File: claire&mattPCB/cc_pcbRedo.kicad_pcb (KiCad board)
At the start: 2 copper layers, 145.2 x 105.1 mm, 89 parts, among them J1 Conn_02x05_Odd_Even, J2 Micro_SD_Card_Det_Hirose_DM3AT, J3 4x4 Keypad, J4 DC-DC_JUMPER, J5 PS_WIRES, J6 PS_BJ, J7 DC-DC Converter, SW1 SW_Push, U1 ESP8266, U2 7in_display_controller, U3 RFID_Scanner, U4 TFT_2.8IN_DISPLAY, U5 74HC14, U6 STM32F091RCTx, U7 MEZD71201AF, U8 TPS56325x, U9 4N28

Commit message: minor changes
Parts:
- added R29: 0, Resistor_SMD:R_0805_2012Metric_Pad1.20x1.40mm_HandSolder, F.Cu at (184.4, 77.7)
- C11, C12: moved to F.Cu
- moved H4 3.34 mm to (82.5, 47.4)
- moved H1 2.14 mm to (82.5, 127.4)
- moved C12 1.59 mm to (176.0, 113.0)
- moved R5 1.42 mm to (122.4, 63.0), turned to 0 degrees
- moved H2 1.39 mm to (207.5, 127.4)
- moved H3 1.31 mm to (207.5, 47.4)
- moved R27 1.18 mm to (140.3, 76.2), turned to 90 degrees
- moved C8 0.87 mm to (122.5, 60.3), turned to 180 degrees
- moved C11 0.83 mm to (176.0, 110.8)
- moved L2 0.75 mm to (172.5, 108.0)
- moved C13 0.15 mm to (174.2, 103.3)
- moved C14 0.15 mm to (174.2, 101.1)
- turned R26 to 90 degrees
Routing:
- net +5V: track 105.7 -> 332.6 mm
- net GND: track 69.8 -> 167.5 mm, vias 10 -> 12
- net +3V3: track 73.9 -> 98.1 mm, vias 5 -> 9
- net 9_GND: track 24.9 -> 39.8 mm, vias 0 -> 1
- net DC_DES: track 11.7 -> 14.5 mm
- net PB14: track 76.8 -> 74.3 mm
- net PB11: track 56.4 -> 57.5 mm
- net Net-(R26-Pad2): track 7.17 -> 6.38 mm
- net /NRST: track 44.6 -> 45.3 mm
- added copper zone on F.Cu, net +3V3
- added copper zone on F.Cu, net GND
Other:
- board size 145.2 x 105.1 mm -> 146.1 x 101.6 mm

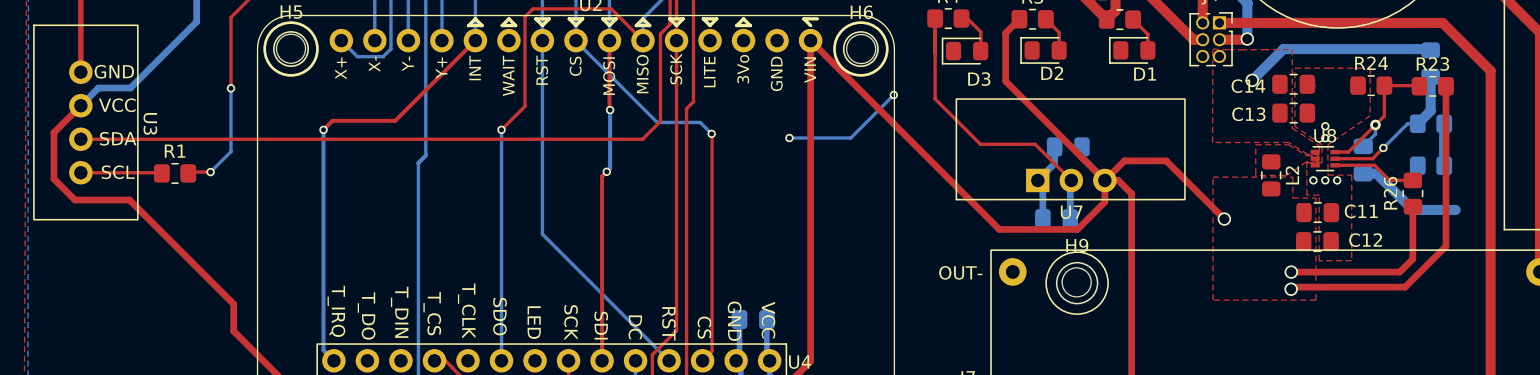
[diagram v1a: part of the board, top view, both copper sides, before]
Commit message: updated schematic with text descriptions for each block. Also, added 0 ohm resistor and 10 ohm current limiting resistor to pcb. Minor changes were made to the designed buck converter circuit.
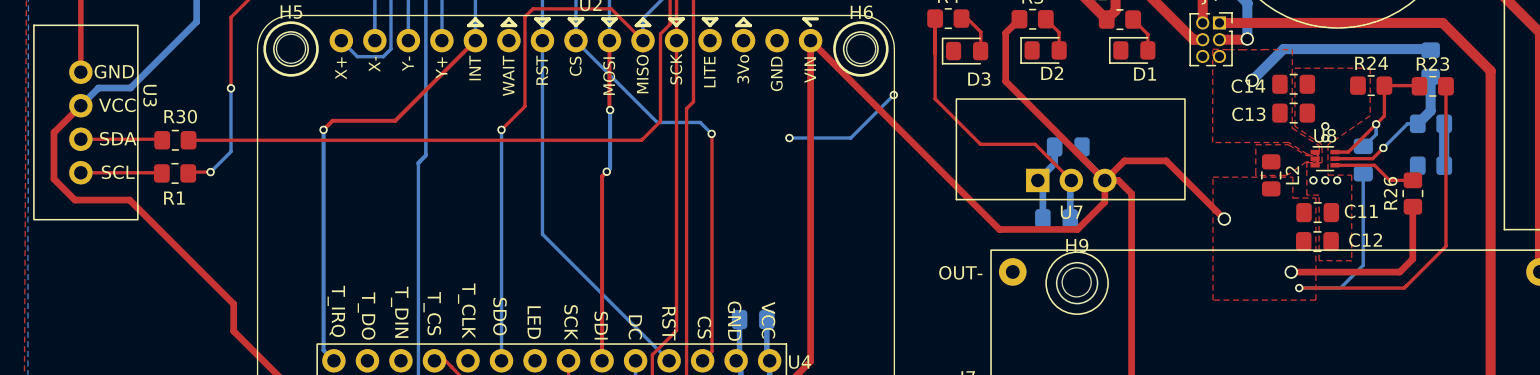
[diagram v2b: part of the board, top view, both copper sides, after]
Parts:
- added R30: 10, Resistor_SMD:R_0805_2012Metric_Pad1.20x1.40mm_HandSolder, F.Cu at (89.5, 105.4)
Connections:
- U3 pad 3: PD2 -> Net-(U3-Pad3)
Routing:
- net PD2: track 67.9 -> 59.8 mm
- net Net-(U3-Pad3): track 0.00 -> 6.19 mm
- net +5V: track 332.6 -> 336.5 mm

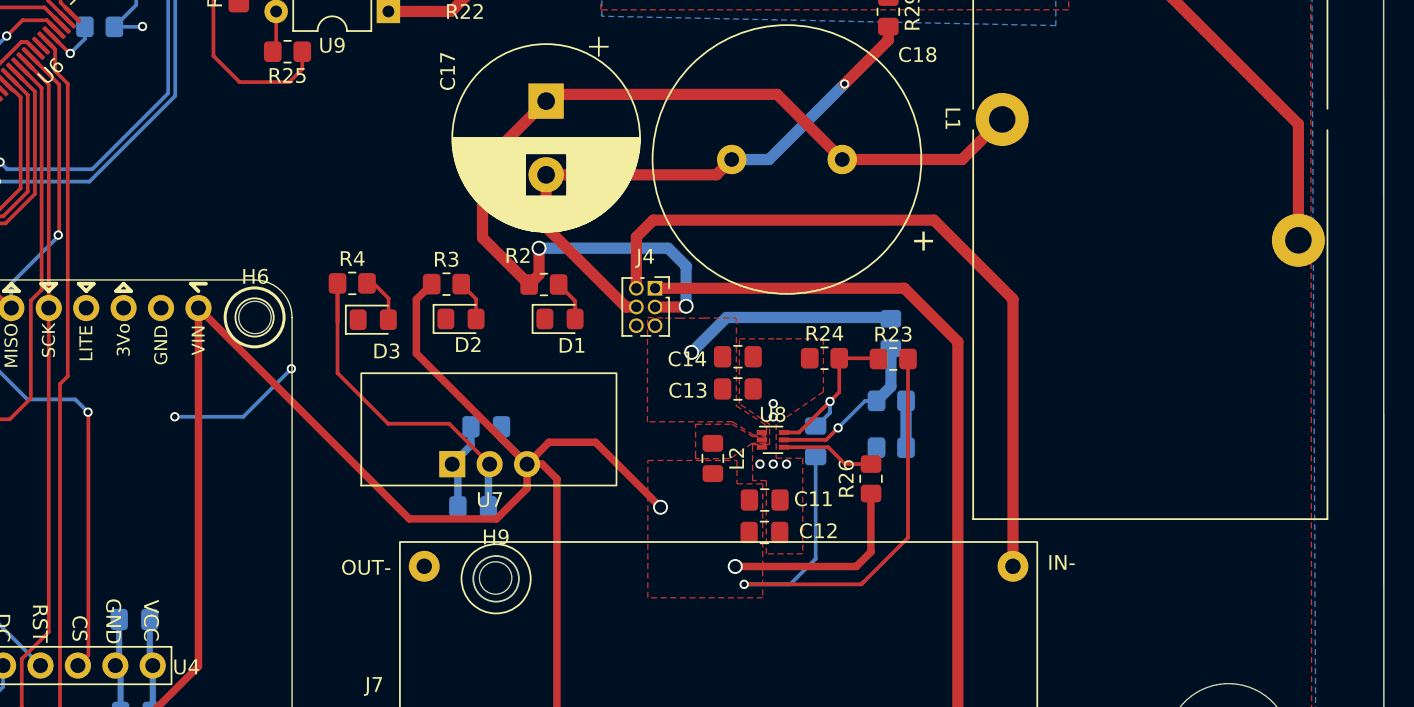
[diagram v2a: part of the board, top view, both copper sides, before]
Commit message: added fantabulous silkscreen names to the board (schmack dab in the middle)
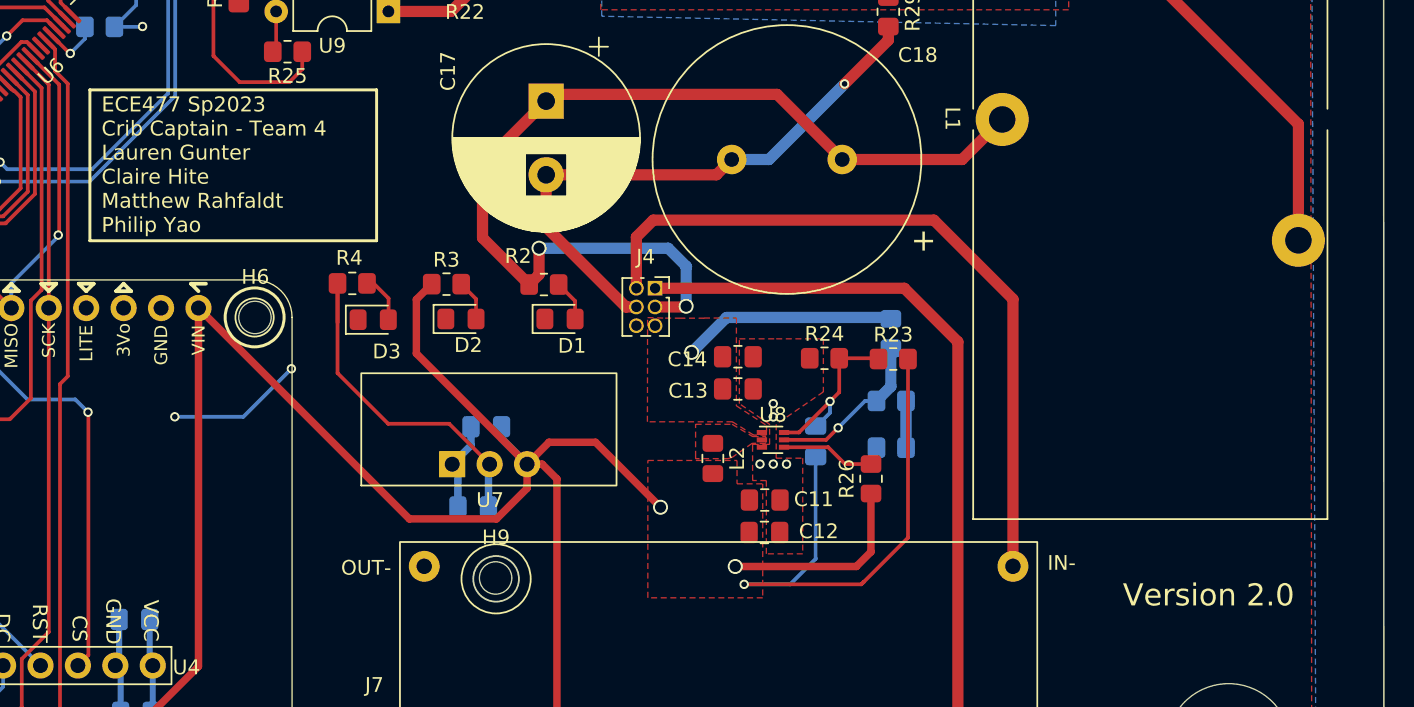
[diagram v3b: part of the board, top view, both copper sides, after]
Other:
- board text added: "ECE477 Sp2023 Crib Captain - Team 4 Lauren Gunter Claire Hite Matthew Rahfaldt Philip Yao"
- board text added: "Version 2.0"
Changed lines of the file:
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@@
     (property "Sheetname" "")
     (attr smd)
-    (fp_text reference "R4" (at 0 -1.65) (layer "F.SilkS")
+    (fp_text reference "R4" (at -0.2032 -1.7272) (layer "F.SilkS")
       (effects (font (size 1 1) (thickness 0.15)))
     )
@@
   )
   (gr_circle (center 130.826559 75.098221) (end 130.826559 75.707821) (layer "F.SilkS") (width 0.15) (fill none))
+  (gr_rect (start 130.2258 83.0072) (end 149.6822 93.2434) (layer "F.SilkS") (width 0.2) (fill none))
   (gr_line (start 209.67 137.94) (end 80.473451 137.94) (layer "Edge.Cuts") (width 0.1))
   (gr_arc (start 209.617374 36.352626) (mid 215.55 38.81) (end 218.007374 44.742626) (layer "Edge.Cuts") (width 0.1))
@@
     (effects (font (size 1.5 1.5) (thickness 0.3)))
   )
+  (gr_text "ECE477 Sp2023\nCrib Captain - Team 4 \nLauren Gunter\nClaire Hite\nMatthew Rahfaldt\nPhilip Yao" (at 131.0132 88.0872) (layer "F.SilkS")
+    (effects (font (size 1.016 1.016) (thickness 0.1905)) (justify left))
+  )
+  (gr_text "Version 2.0" (at 206.1464 117.2972) (layer "F.SilkS")
+    (effects (font (size 1.5 1.5) (thickness 0.3)))
+  )

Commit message: no DRC warnings
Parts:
- moved C12 0.29 mm to (176.0, 112.8)
- moved C11 0.10 mm to (176.0, 110.7)
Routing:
- net +3V3: track 98.1 -> 118.8 mm
- net GND: track 167.3 -> 184.4 mm, vias 12 -> 13
- net PB5: track 45.8 -> 62.5 mm
- net PB4: track 57.0 -> 70.0 mm
- net PB3: track 54.9 -> 64.5 mm
- net VAC_GND: track 37.8 -> 47.3 mm
- net PB14: track 74.3 -> 71.7 mm
- net PB7: track 71.4 -> 73.1 mm

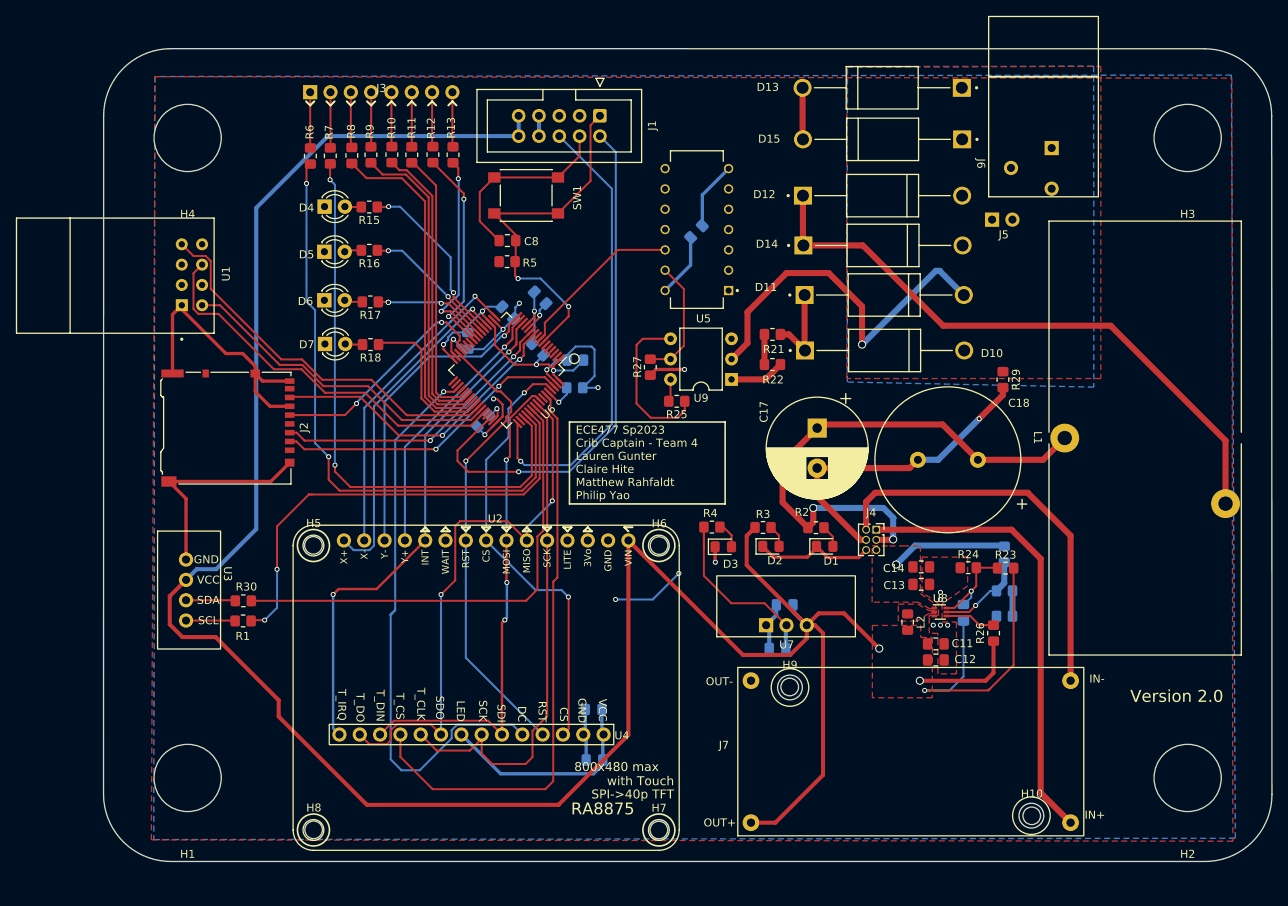
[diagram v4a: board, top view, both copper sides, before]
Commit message: diodes and vias w labels added
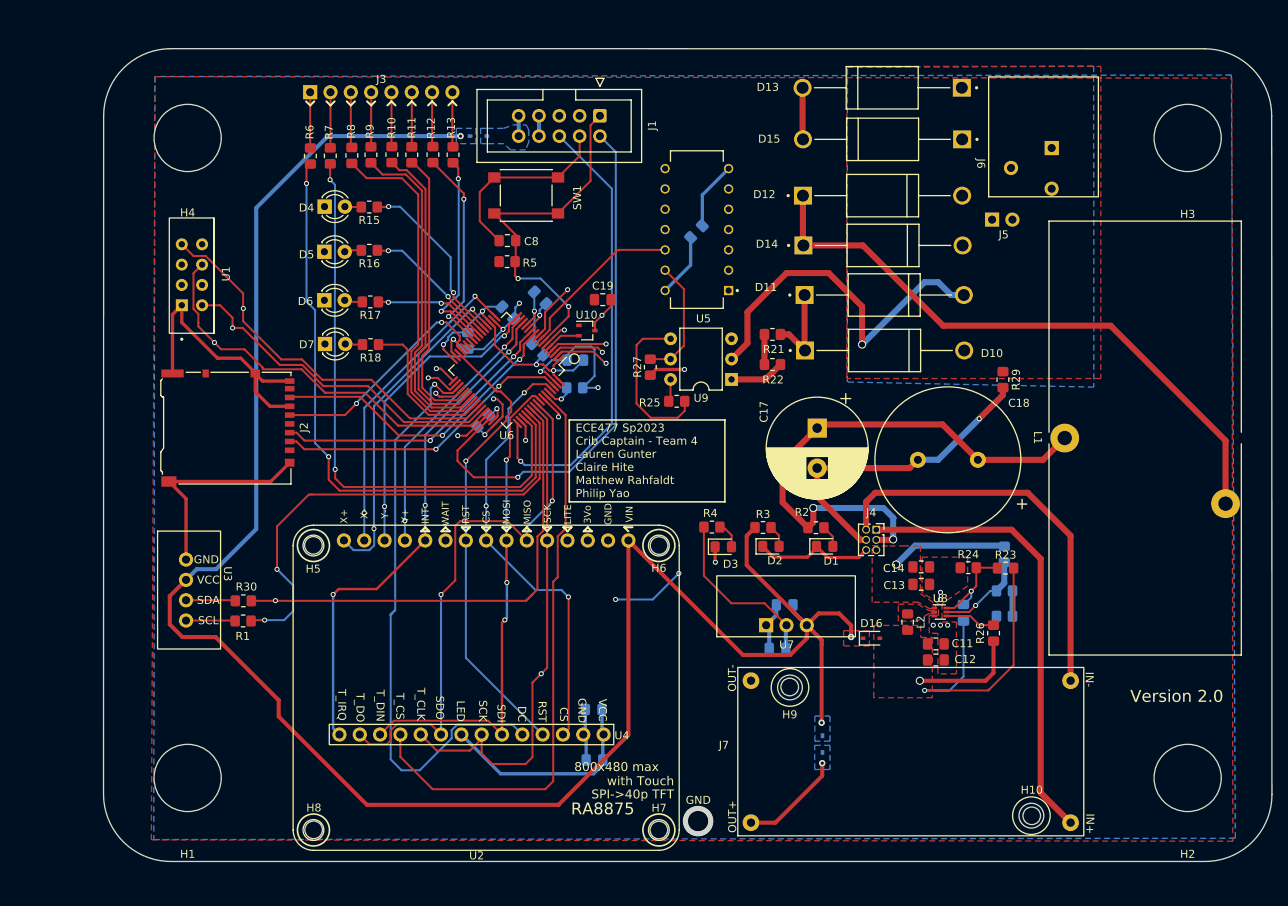
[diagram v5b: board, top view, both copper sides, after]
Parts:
- added C19: .1uF, Capacitor_SMD:C_0805_2012Metric_Pad1.18x1.45mm_HandSolder, F.Cu at (134.4, 67.7)
- added D16: BAT60JFILM, Diode_SMD:D_SOD-323, F.Cu at (168.0, 110.0)
- added D8: BAT60JFILM, Diode_SMD:D_SOD-323, B.Cu at (118.8, 47.3)
- added D9: BAT60JFILM, Diode_SMD:D_SOD-323, B.Cu at (161.8, 123.3)
- added U10: MAX7375AXR805, Package_TO_SOT_SMD:SOT-323_SC-70, F.Cu at (132.4, 71.6)
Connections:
- C11 pad 1: +5V -> Net-(C11-Pad1)
- C12 pad 1: +5V -> Net-(C11-Pad1)
- C16 pad 1: +5V -> Net-(C11-Pad1)
- J1 pad 10: +5V -> /U5V
- J1 pad 9: +5V -> /U5V
- J7 pad 3: +5V -> Net-(J7-Pad3)
- L2 pad 2: +5V -> Net-(C11-Pad1)
- R23 pad 2: +5V -> Net-(C11-Pad1)
- R26 pad 1: +5V -> Net-(C11-Pad1)
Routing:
- net +5V: track 336.5 -> 253.9 mm
- net Net-(C11-Pad1): track 0.00 -> 50.8 mm, vias 0 -> 2
- net Net-(J7-Pad3): track 0.00 -> 12.9 mm, vias 0 -> 1
- net /PC1: track 0.00 -> 7.43 mm, vias 0 -> 1
- net /PC15: track 0.00 -> 7.19 mm, vias 0 -> 1
- net /PC13: track 0.00 -> 6.98 mm, vias 0 -> 1
- net /PC14: track 0.00 -> 6.57 mm, vias 0 -> 1
- net GND: track 184.4 -> 190.7 mm, vias 13 -> 15
- net PC10: track 79.0 -> 73.2 mm
- net /PA12: track 0.00 -> 4.76 mm, vias 0 -> 1
- net /PF0: track 0.00 -> 4.42 mm
- net /PB13: track 0.00 -> 4.37 mm, vias 0 -> 1
- net /PB15: track 0.00 -> 3.79 mm, vias 0 -> 1
- net /PB6: track 0.00 -> 3.17 mm, vias 0 -> 1
- net /PF1: track 0.00 -> 3.11 mm, vias 0 -> 1
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- added copper zone on B.Cu, net +5V
- added copper zone on B.Cu, net /U5V
- added copper zone on F.Cu, net Net-(C11-Pad1)
- added copper zone on B.Cu, net Net-(J7-Pad3)
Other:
- board text added: "GND"
- board text added: "PA0"
- board text added: "PA1"
- board text added: "PA10"
- board text added: "PA11"
- board text added: "PA12"
- board text added: "PA13"
- board text added: "PA14"
- board text added: "PA15"
- board text added: "PA2"
- board text added: "PA3"
- board text added: "PA4"
- board text added: "PA9"
- board text added: "PB10"
- board text added: "PB11"
- board text added: "PB12"
- board text added: "PB13"
- board text added: "PB14"
- board text added: "PB15"
- board text added: "PB3"
- board text added: "PB4"
- board text added: "PB5"
- board text added: "PB6"
- board text added: "PB8"
- board text added: "PB9"
- board text added: "PC1"
- board text added: "PC10"
- board text added: "PC11"
- board text added: "PC12"
- board text added: "PC13"
- board text added: "PC14"
- board text added: "PC15"
- board text added: "PC2"
- board text added: "PC3"
- board text added: "PD2"
- board text added: "PF1"
- board text added: "RST"
- board text added: "RX"
- board text added: "TX"

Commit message: pcb finalization
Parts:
- J4: footprint Connector_PinSocket_1.27mm:PinSocket_2x03_P1.27mm_Vertical -> Connector_PinSocket_2.54mm:PinSocket_2x03_P2.54mm_Vertical
- moved J4 1.17 mm to (168.4, 95.3)
- moved H10 0.36 mm to (188.2, 132.6)
- moved H9 0.35 mm to (157.6, 115.8)
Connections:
- U5 pad 12: PC0 -> PC13
- U6 pad 2: /PC13 -> PC13
- U6 pad 8: PC0 -> /PC0
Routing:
- net PC13: track 0.00 -> 24.2 mm, vias 0 -> 1
- net PC0: track 21.1 -> 0.00 mm
- net /PC13: track 6.98 -> 0.00 mm, vias 1 -> 0
- net +3V3: track 116.0 -> 121.4 mm
- net /PC1: track 7.43 -> 5.72 mm
- net GND: track 190.7 -> 189.0 mm
- net +9V: track 68.7 -> 67.6 mm, vias 2 -> 0
- net 9_GND: track 39.8 -> 38.9 mm
- net DC_DES: track 14.5 -> 13.7 mm
- net /NRST: track 45.3 -> 46.1 mm, vias 2 -> 0
- net DC_MOD: track 56.6 -> 57.2 mm
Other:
- board text added: ":-$"
- board text added: ":-o"
- board text added: "Dedicated to: Benji Henny"
- board text added: "Direct enemy of: Big Pocket/Handbag Non-ECE477 Classes Truth or Consequences, NM"
- board text added: "Don't mind me J a silly lil' PCB"
- board text added: "PCB"
- board text added: "PCB my valentine, because you've got all the right components!"
- board text added: "PCB who?"
- board text added: "Peace <3 Walmart Sparkling Water"
- board text added: "Sponsored by: McDonald's OHANA Phillip's Corner (Jail)"
- board text added: "Team Selena all the way"
- board text added: "Warning: CribCaptain(TM) CANNOT do your dishes, but it CAN make your roommates do them"
- board text added: "Why did the pirate PCB, Crib Captain, decide to get a roommate? Because it wanted someone to {dblquote}board{dblquote} with!"
- board text added: "knock-knock"
- board text added: "the Doo-Hickey (TM)"
- board text added: "who's there?"
- board text added: "word."
